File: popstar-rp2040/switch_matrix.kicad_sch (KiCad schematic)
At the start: 151 parts, among them SW10 MX_SW_solder, SW11 MX_SW_solder, SW12 MX_SW_solder, SW13 MX_SW_solder, SW14 MX_SW_solder, SW15 MX_SW_solder, SW16 MX_SW_solder, SW17 MX_SW_solder, SW18 MX_SW_solder, SW19 MX_SW_solder, SW2 MX_SW_solder, SW20 MX_SW_solder, SW21 MX_SW_solder, SW22 MX_SW_solder, SW23 MX_SW_solder, SW24 MX_SW_solder, SW25 MX_SW_solder, SW26 MX_SW_solder, SW27 MX_SW_solder, SW28 MX_SW_solder, SW29 MX_SW_solder, SW3 MX_SW_solder, SW30 MX_SW_solder, SW31 MX_SW_solder, SW32 MX_SW_solder, SW33 MX_SW_solder, SW34 MX_SW_solder, SW35 MX_SW_solder, SW36 MX_SW_solder, SW37 MX_SW_solder, SW38 MX_SW_solder, SW39 MX_SW_solder, SW4 MX_SW_solder, SW40 MX_SW_solder, SW41 MX_SW_solder, SW42 MX_SW_solder, SW43 MX_SW_solder, SW44 MX_SW_solder, SW45 MX_SW_solder, SW46 MX_SW_solder, SW47 MX_SW_solder, SW48 MX_SW_solder, SW49 MX_SW_solder, SW5 MX_SW_solder, SW50 MX_SW_solder, SW51 MX_SW_solder, SW52 MX_SW_solder, SW53 MX_SW_solder, SW54 MX_SW_solder, SW55 MX_SW_solder, SW56 MX_SW_solder, SW57 MX_SW_solder, SW58 MX_SW_solder, SW59 MX_SW_solder, SW6 MX_SW_solder, SW60 MX_SW_solder, SW61 MX_SW_solder, SW62 MX_SW_solder, SW7 MX_SW_solder, SW8 MX_SW_solder, SW9 MX_SW_solder, U5 74AHCT1G125

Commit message: Added LCSC part for LEDs, gerber files for prod
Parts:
- D1, D10, D11, D12, D2, D3, D4, D5, D6, D7, D8, D9: LCSC (none) -> C965556
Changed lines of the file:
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@@
       (effects (font (size 1.27 1.27)) (justify left top) hide)
     )
+    (property "LCSC" "C965556" (at 56.515 149.225 0)
+      (effects (font (size 1.27 1.27)) hide)
+    )
     (pin "1")
     (pin "2")
@@
       (effects (font (size 1.27 1.27)) (justify left top) hide)
     )
+    (property "LCSC" "C965556" (at 104.14 149.225 0)
+      (effects (font (size 1.27 1.27)) hide)
+    )
     (pin "1")
     (pin "2")
@@
       (effects (font (size 1.27 1.27)) (justify left top) hide)
     )
+    (property "LCSC" "C965556" (at 40.64 149.225 0)
+      (effects (font (size 1.27 1.27)) hide)
+    )
     (pin "1")
     (pin "2")
@@
       (effects (font (size 1.27 1.27)) (justify left top) hide)
     )
+    (property "LCSC" "C965556" (at 199.39 149.225 0)
+      (effects (font (size 1.27 1.27)) hide)
+    )
     (pin "1")
     (pin "2")
@@
       (effects (font (size 1.27 1.27)) (justify left top) hide)
     )
+    (property "LCSC" "C965556" (at 72.39 149.225 0)
+      (effects (font (size 1.27 1.27)) hide)
+    )
     (pin "1")
     (pin "2")
@@
       (effects (font (size 1.27 1.27)) (justify left top) hide)
     )
+    (property "LCSC" "C965556" (at 120.015 149.225 0)
+      (effects (font (size 1.27 1.27)) hide)
+    )
     (pin "1")
     (pin "2")
@@
       (effects (font (size 1.27 1.27)) (justify left top) hide)
     )
+    (property "LCSC" "C965556" (at 183.515 149.225 0)
+      (effects (font (size 1.27 1.27)) hide)
+    )
     (pin "1")
     (pin "2")
@@
       (effects (font (size 1.27 1.27)) (justify left top) hide)
     )
+    (property "LCSC" "C965556" (at 88.265 149.225 0)
+      (effects (font (size 1.27 1.27)) hide)
+    )
     (pin "1")
     (pin "2")
@@
       (effects (font (size 1.27 1.27)) (justify left top) hide)
     )
+    (property "LCSC" "C965556" (at 167.64 149.225 0)
+      (effects (font (size 1.27 1.27)) hide)
+    )
     (pin "1")
     (pin "2")
@@
       (effects (font (size 1.27 1.27)) (justify left top) hide)
     )
+    (property "LCSC" "C965556" (at 215.265 149.225 0)
+      (effects (font (size 1.27 1.27)) hide)
+    )
     (pin "1")
     (pin "2")
@@
       (effects (font (size 1.27 1.27)) (justify left top) hide)
     )
+    (property "LCSC" "C965556" (at 135.89 149.225 0)
+      (effects (font (size 1.27 1.27)) hide)
+    )
     (pin "1")
     (pin "2")
@@
       (effects (font (size 1.27 1.27)) (justify left top) hide)
     )
+    (property "LCSC" "C965556" (at 151.765 149.225 0)
+      (effects (font (size 1.27 1.27)) hide)
+    )
     (pin "1")

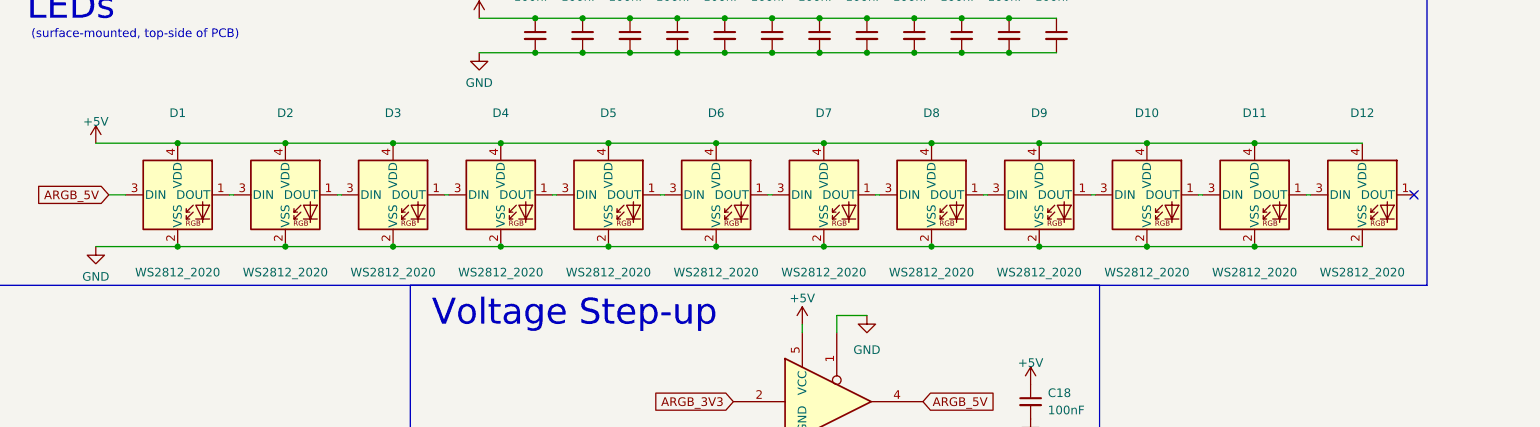
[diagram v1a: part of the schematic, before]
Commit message: Updated LEDs to use SK6812MINI-E (rev mount) in schematic. PCB design update WIP.
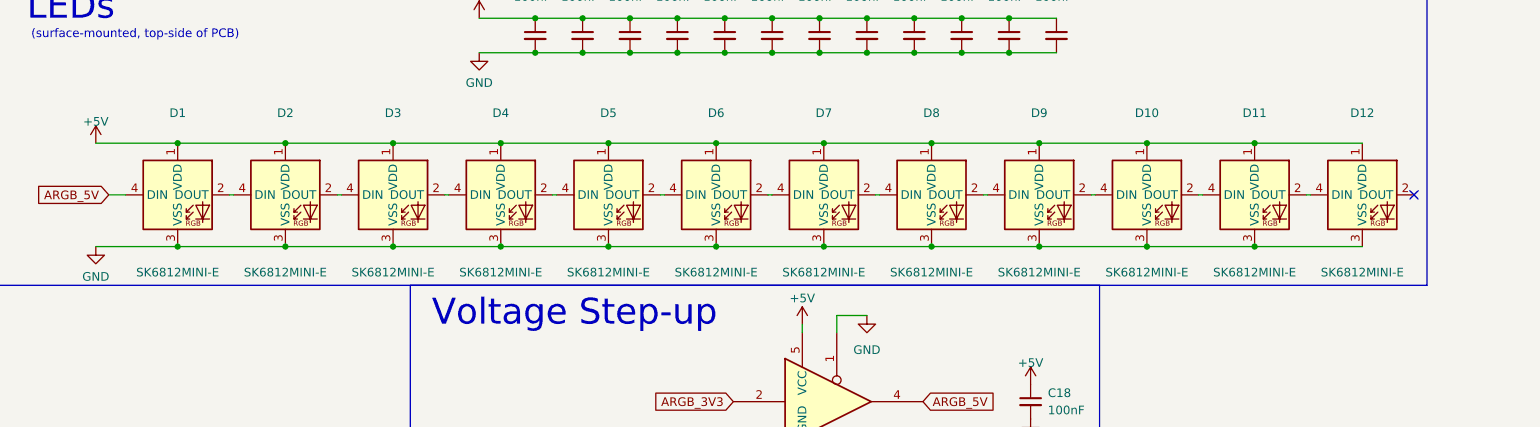
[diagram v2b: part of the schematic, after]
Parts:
- removed D10, D11, D12, D3, D4, D5, D6, D7, D8, D9: WS2812_2020, marbastlib-various:LED_WS2812_2020, symbol marbastlib-various:WS2812_2020
- added D10, D11, D12, D3, D4, D5, D6, D7, D8, D9: SK6812MINI-E, marbastlib-various:LED_6028R, symbol marbastlib-various:SK6812MINI-E
- D1, D2: value WS2812_2020 -> SK6812MINI-E; footprint marbastlib-various:LED_WS2812_2020 -> marbastlib-various:LED_6028R; symbol marbastlib-various:WS2812_2020 -> marbastlib-various:SK6812MINI-E; LCSC C965556 -> C5149201
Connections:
- net +5V: now also D1.1 (VDD), D2.1 (VDD), D10.1 (VDD), D11.1 (VDD), D12.1 (VDD), D3.1 (VDD), D4.1 (VDD), D5.1 (VDD), D6.1 (VDD), D7.1 (VDD), D8.1 (VDD), D9.1 (VDD); no longer D1.4 (VDD), D2.4 (VDD)
- net ARGB_5V: now also D1.4 (DIN); no longer D1.3 (DIN)
- net GND: now also D1.3 (VSS), D2.3 (VSS), D10.3 (VSS), D11.3 (VSS), D12.3 (VSS), D3.3 (VSS), D4.3 (VSS), D5.3 (VSS), D6.3 (VSS), D7.3 (VSS), D8.3 (VSS), D9.3 (VSS); no longer D1.2 (VSS), D2.2 (VSS)
- new net: D2.2 (DOUT), D3.4 (DIN)
- new net: D1.2 (DOUT), D2.4 (DIN)
- new net: D11.2 (DOUT), D12.4 (DIN)
- new net: D3.2 (DOUT), D4.4 (DIN)
- new net: D5.2 (DOUT), D6.4 (DIN)
- new net: D4.2 (DOUT), D5.4 (DIN)
- new net: D10.2 (DOUT), D11.4 (DIN)
- new net: D10.4 (DIN), D9.2 (DOUT)
- new net: D8.2 (DOUT), D9.4 (DIN)
- new net: D7.2 (DOUT), D8.4 (DIN)
- new net: D6.2 (DOUT), D7.4 (DIN)

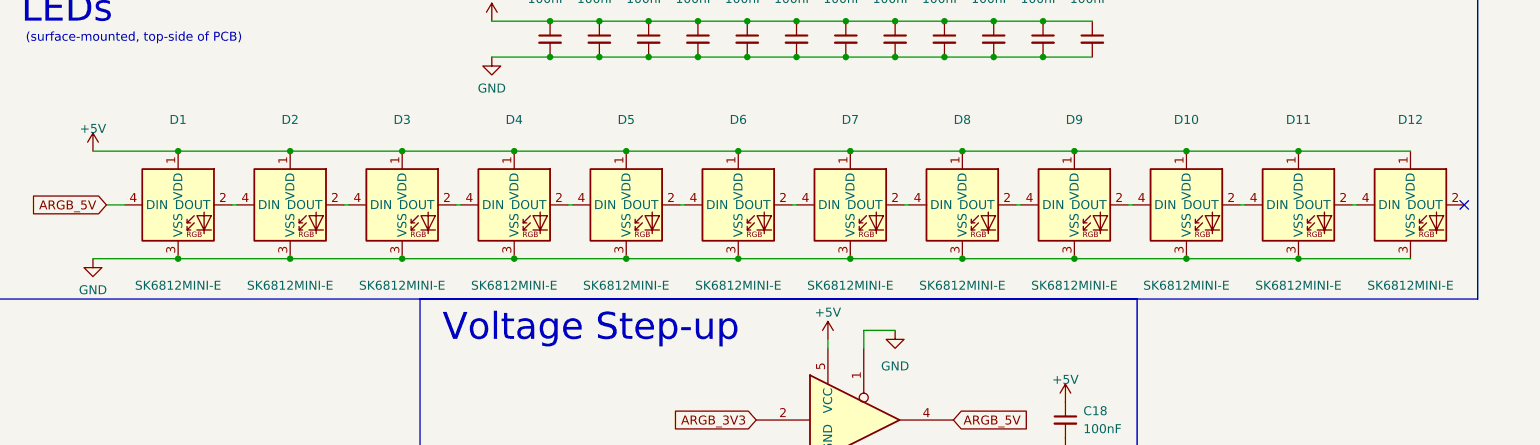
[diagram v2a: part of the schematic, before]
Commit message: Used unedit footprints for LEDs
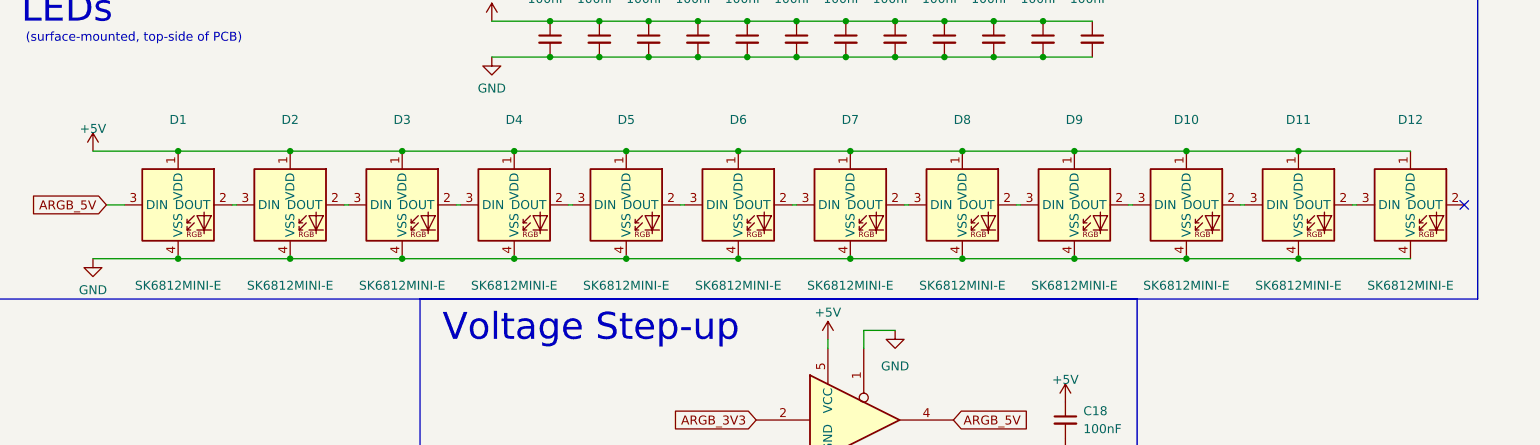
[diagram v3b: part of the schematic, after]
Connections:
- net ARGB_5V: now also D1.3 (DIN); no longer D1.4 (DIN)
- net GND: now also D1.4 (VSS), D10.4 (VSS), D11.4 (VSS), D12.4 (VSS), D2.4 (VSS), D3.4 (VSS), D4.4 (VSS), D5.4 (VSS), D6.4 (VSS), D7.4 (VSS), D8.4 (VSS), D9.4 (VSS); no longer D1.3 (VSS), D10.3 (VSS), D11.3 (VSS), D12.3 (VSS), D2.3 (VSS), D3.3 (VSS), D4.3 (VSS), D5.3 (VSS), D6.3 (VSS), D7.3 (VSS), D8.3 (VSS), D9.3 (VSS)
- net at D2.2 (DOUT): now also D3.3 (DIN); no longer D3.4 (DIN)
- net at D1.2 (DOUT): now also D2.3 (DIN); no longer D2.4 (DIN)
- net at D11.2 (DOUT): now also D12.3 (DIN); no longer D12.4 (DIN)
- net at D3.2 (DOUT): now also D4.3 (DIN); no longer D4.4 (DIN)
- net at D5.2 (DOUT): now also D6.3 (DIN); no longer D6.4 (DIN)
- net at D4.2 (DOUT): now also D5.3 (DIN); no longer D5.4 (DIN)
- net at D10.2 (DOUT): now also D11.3 (DIN); no longer D11.4 (DIN)
- net at D9.2 (DOUT): now also D10.3 (DIN); no longer D10.4 (DIN)
- net at D8.2 (DOUT): now also D9.3 (DIN); no longer D9.4 (DIN)
- net at D7.2 (DOUT): now also D8.3 (DIN); no longer D8.4 (DIN)
- net at D6.2 (DOUT): now also D7.3 (DIN); no longer D7.4 (DIN)
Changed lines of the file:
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@@
     )
   )
-  (symbol (lib_name "SK6812MINI-E_1") (lib_id "marbastlib-various:SK6812MINI-E") (at 56.515 149.225 0) (unit 1)
+  (symbol (lib_name "SK6812MINI-E_2") (lib_id "marbastlib-various:SK6812MINI-E") (at 56.515 149.225 0) (unit 1)
     (in_bom yes) (on_board yes) (dnp no)
     (property "Reference" "D2" (at 56.515 137.16 0)
@@
     (pin "1")
     (pin "2")
-    (pin "4")
     (pin "3")
+    (pin "4")
     (instances
       (project "popstar"
@@
     )
   )
-  (symbol (lib_name "SK6812MINI-E_1") (lib_id "marbastlib-various:SK6812MINI-E") (at 72.39 149.225 0) (unit 1)
+  (symbol (lib_name "SK6812MINI-E_3") (lib_id "marbastlib-various:SK6812MINI-E") (at 72.39 149.225 0) (unit 1)
     (in_bom yes) (on_board yes) (dnp no)
     (property "Reference" "D3" (at 72.39 137.16 0)
@@
     )
   )
-  (symbol (lib_name "SK6812MINI-E_1") (lib_id "marbastlib-various:SK6812MINI-E") (at 104.14 149.225 0) (unit 1)
+  (symbol (lib_name "SK6812MINI-E_5") (lib_id "marbastlib-various:SK6812MINI-E") (at 104.14 149.225 0) (unit 1)
     (in_bom yes) (on_board yes) (dnp no)
     (property "Reference" "D5" (at 104.14 137.16 0)
@@
     )
   )
-  (symbol (lib_name "SK6812MINI-E_1") (lib_id "marbastlib-various:SK6812MINI-E") (at 183.515 149.225 0) (unit 1)
+  (symbol (lib_name "SK6812MINI-E_10") (lib_id "marbastlib-various:SK6812MINI-E") (at 183.515 149.225 0) (unit 1)
     (in_bom yes) (on_board yes) (dnp no)
     (property "Reference" "D10" (at 183.515 137.16 0)
@@
     )
   )
-  (symbol (lib_name "SK6812MINI-E_1") (lib_id "marbastlib-various:SK6812MINI-E") (at 88.265 149.225 0) (unit 1)
+  (symbol (lib_name "SK6812MINI-E_4") (lib_id "marbastlib-various:SK6812MINI-E") (at 88.265 149.225 0) (unit 1)
     (in_bom yes) (on_board yes) (dnp no)
     (property "Reference" "D4" (at 88.265 137.16 0)
@@
     (pin "1")
     (pin "2")
-    (pin "3")
     (pin "4")
+    (pin "3")
     (instances
       (project "popstar"
@@
     )
   )
-  (symbol (lib_name "SK6812MINI-E_1") (lib_id "marbastlib-various:SK6812MINI-E") (at 151.765 149.225 0) (unit 1)
+  (symbol (lib_name "SK6812MINI-E_8") (lib_id "marbastlib-various:SK6812MINI-E") (at 151.765 149.225 0) (unit 1)
     (in_bom yes) (on_board yes) (dnp no)
     (property "Reference" "D8" (at 151.765 137.16 0)
@@
     )
   )
-  (symbol (lib_name "SK6812MINI-E_1") (lib_id "marbastlib-various:SK6812MINI-E") (at 167.64 149.225 0) (unit 1)
+  (symbol (lib_name "SK6812MINI-E_9") (lib_id "marbastlib-various:SK6812MINI-E") (at 167.64 149.225 0) (unit 1)
     (in_bom yes) (on_board yes) (dnp no)
     (property "Reference" "D9" (at 167.64 137.16 0)
@@
     )
   )
-  (symbol (lib_name "SK6812MINI-E_1") (lib_id "marbastlib-various:SK6812MINI-E") (at 120.015 149.225 0) (unit 1)
+  (symbol (lib_name "SK6812MINI-E_6") (lib_id "marbastlib-various:SK6812MINI-E") (at 120.015 149.225 0) (unit 1)
     (in_bom yes) (on_board yes) (dnp no)
     (property "Reference" "D6" (at 120.015 137.16 0)
@@
     )
   )
-  (symbol (lib_name "SK6812MINI-E_1") (lib_id "marbastlib-various:SK6812MINI-E") (at 199.39 149.225 0) (unit 1)
+  (symbol (lib_name "SK6812MINI-E_11") (lib_id "marbastlib-various:SK6812MINI-E") (at 199.39 149.225 0) (unit 1)
     (in_bom yes) (on_board yes) (dnp no)
     (property "Reference" "D11" (at 199.39 137.16 0)
@@
     )
   )
-  (symbol (lib_name "SK6812MINI-E_1") (lib_id "marbastlib-various:SK6812MINI-E") (at 135.89 149.225 0) (unit 1)
+  (symbol (lib_name "SK6812MINI-E_7") (lib_id "marbastlib-various:SK6812MINI-E") (at 135.89 149.225 0) (unit 1)
     (in_bom yes) (on_board yes) (dnp no)
     (property "Reference" "D7" (at 135.89 137.16 0)
